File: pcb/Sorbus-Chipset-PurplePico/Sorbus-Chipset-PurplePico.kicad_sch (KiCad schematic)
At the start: 4 parts, among them J1 Conn_01x32_Pin, J2 Conn_01x20_Pin, J3 Conn_01x20_Pin, J4 Conn_01x05_Pin

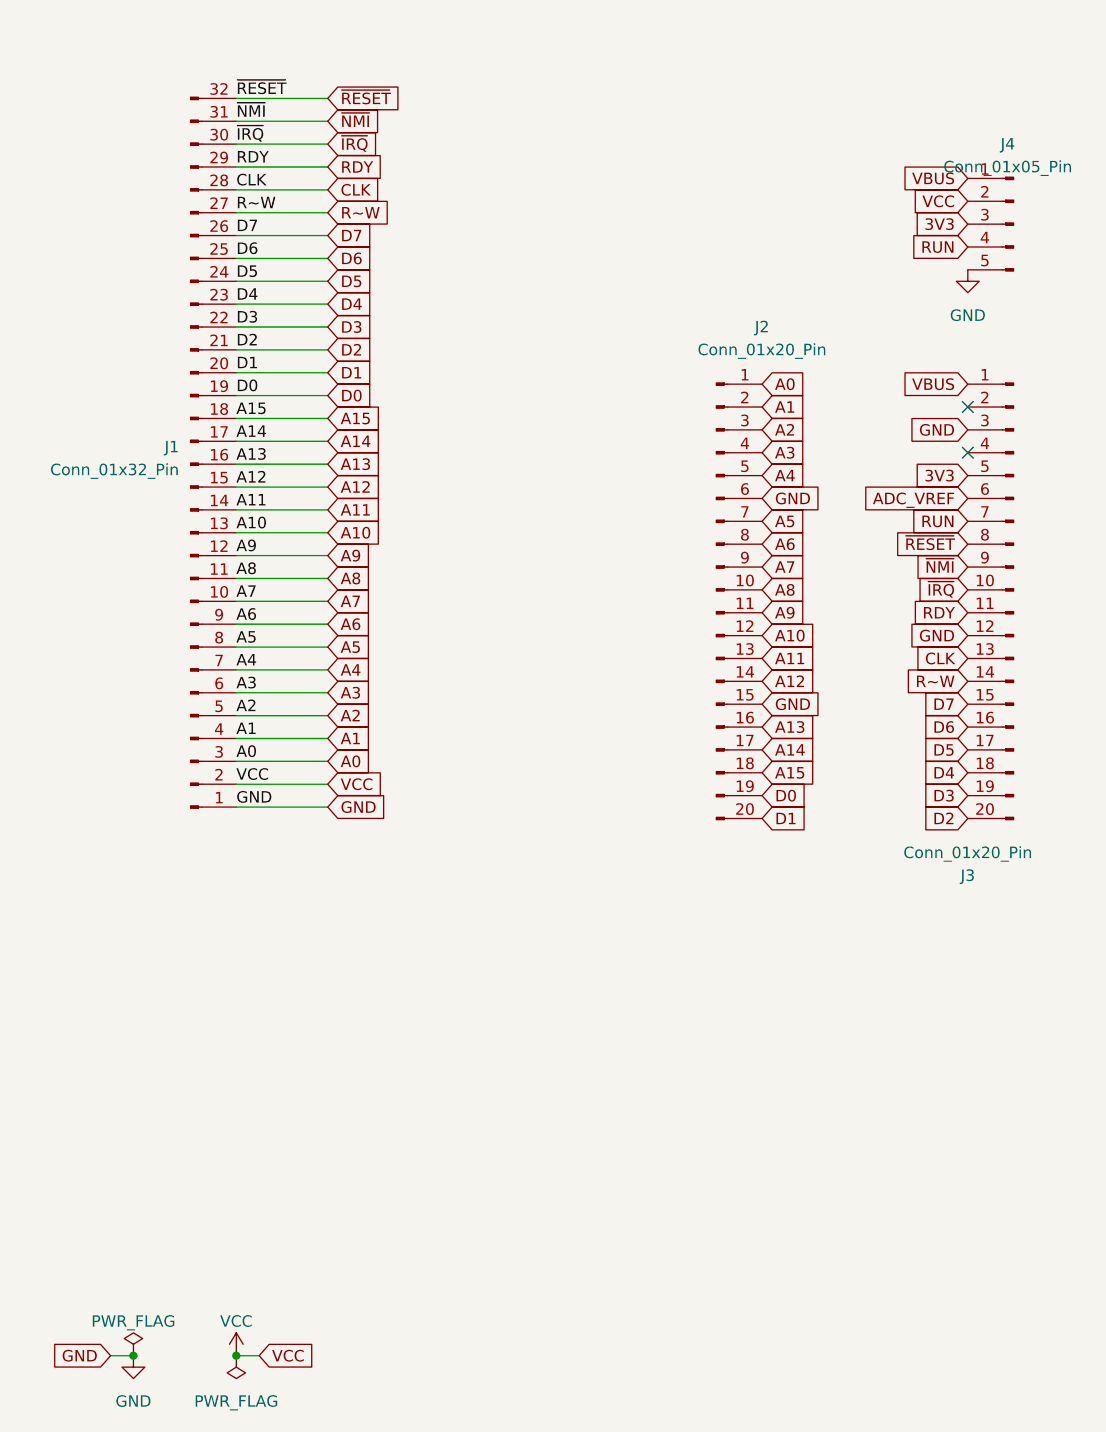
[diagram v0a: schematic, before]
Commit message: updated PCB design - added decoupling capacitor to 65C02 board - replaced simple connectors with real RP2040 Purple component - also updated gerber file and PDF exports from PCB changes - fixed problem in bare build
Signed-off-by: Sven Oliver Moll <svolli@svolli.de>
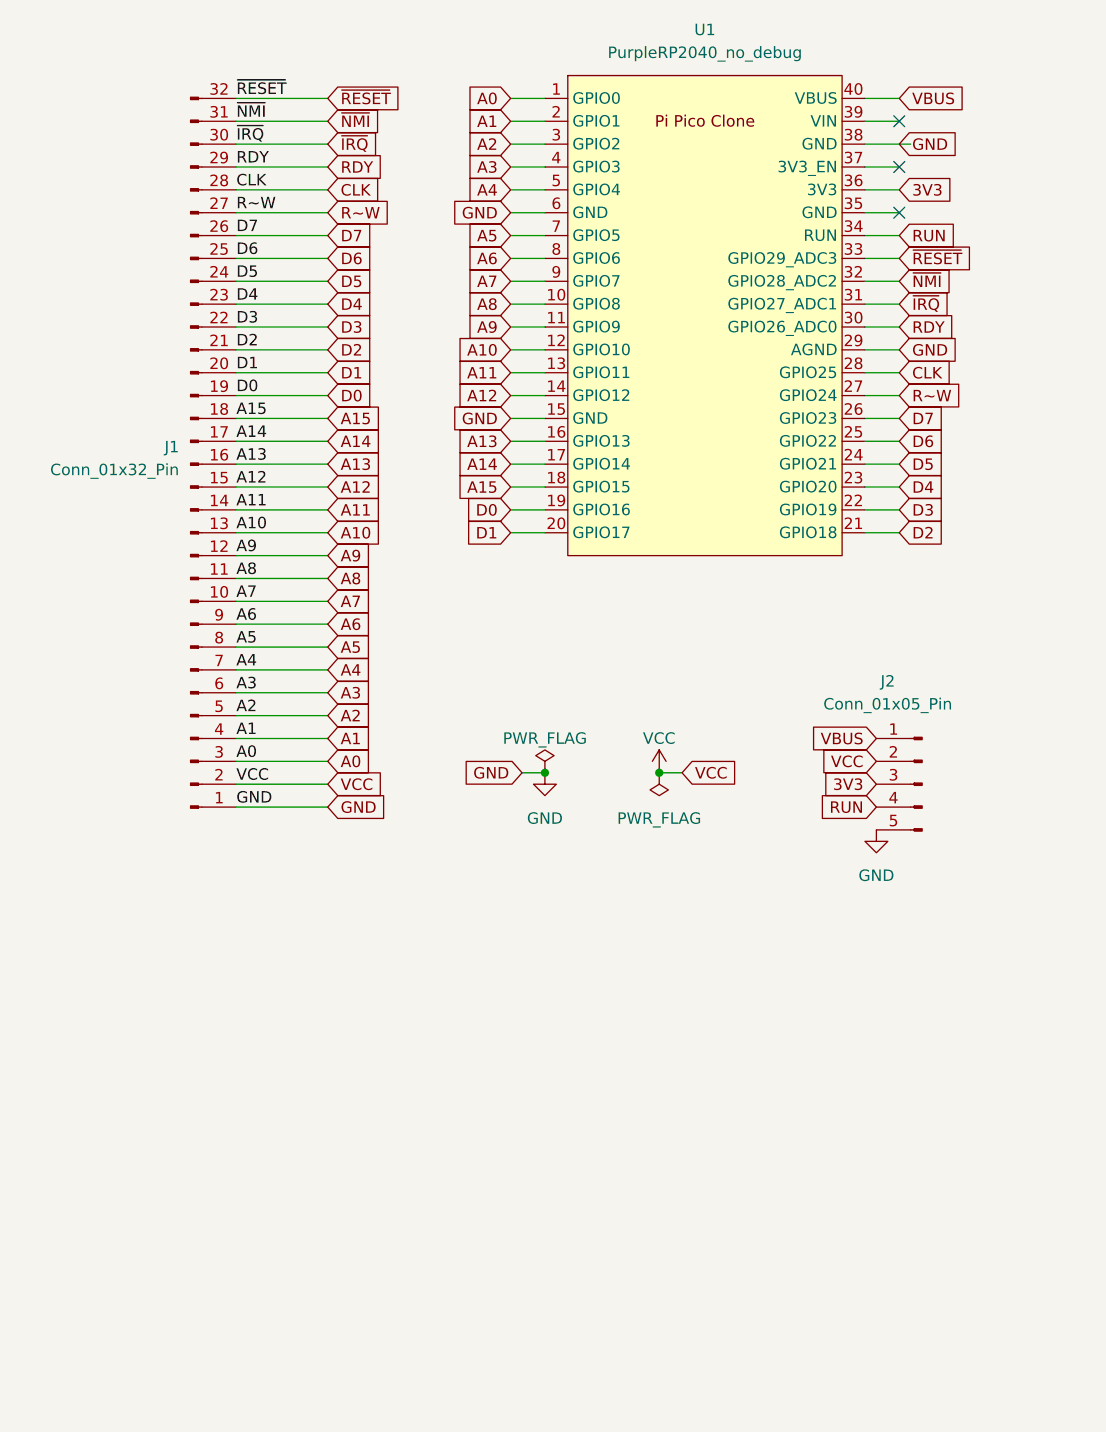
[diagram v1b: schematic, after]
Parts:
- removed J2, J3: Conn_01x20_Pin, Connector_PinHeader_2.54mm:PinHeader_1x20_P2.54mm_Vertical, symbol Connector:Conn_01x20_Pin
- added U1: PurpleRP2040_no_debug, MCU_RaspberryPi_and_Boards:RPi_RP2040Purple_SMD_TH_no_debug, symbol MCU_RaspberryPi_and_Boards:PurpleRP2040_no_debug
- renumbered J4 to J2
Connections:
- net 3V3: now also U1.36 (3V3)
- net A0: now also U1.1 (GPIO0)
- net A1: now also U1.2 (GPIO1)
- net A10: now also U1.12 (GPIO10)
- net A11: now also U1.13 (GPIO11)
- net A12: now also U1.14 (GPIO12)
- net A13: now also U1.16 (GPIO13)
- net A14: now also U1.17 (GPIO14)
- net A15: now also U1.18 (GPIO15)
- net A2: now also U1.3 (GPIO2)
- net A3: now also U1.4 (GPIO3)
- net A4: now also U1.5 (GPIO4)
- net A5: now also U1.7 (GPIO5)
- net A6: now also U1.8 (GPIO6)
- net A7: now also U1.9 (GPIO7)
- net A8: now also U1.10 (GPIO8)
- net A9: now also U1.11 (GPIO9)
- net CLK: now also U1.28 (GPIO25)
- net D0: now also U1.19 (GPIO16)
- net D1: now also U1.20 (GPIO17)
- net D2: now also U1.21 (GPIO18)
- net D3: now also U1.22 (GPIO19)
- net D4: now also U1.23 (GPIO20)
- net D5: now also U1.24 (GPIO21)
- net D6: now also U1.25 (GPIO22)
- net D7: now also U1.26 (GPIO23)
- net GND: now also U1.15 (GND), U1.29 (AGND), U1.38 (GND), U1.6 (GND)
- net RDY: now also U1.30 (GPIO26_ADC0)
- net RUN: now also U1.34 (RUN)
- net R~W: now also U1.27 (GPIO24)
- net VBUS: now also U1.40 (VBUS)
- net ~{IRQ}: now also U1.31 (GPIO27_ADC1)
- net ~{NMI}: now also U1.32 (GPIO28_ADC2)
- net ~{RESET}: now also U1.33 (GPIO29_ADC3)
- no-connect marks 2 -> 3
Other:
- title: (none) -> Sorbus Computer RP2040 Purple
- moved on the sheet: J2
